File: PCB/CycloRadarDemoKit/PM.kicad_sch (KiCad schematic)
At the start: 47 parts, among them J401 20-16V Supply Voltage, Q401 SI2309CDS, U401 INA3221, U402 RT8259, U403 TPS2121RUXR, U404 AP63205WU, U405 AP63203WU

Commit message: more components fthprnt added
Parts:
- L401: footprint (none) -> Inductor_SMD:L_Changjiang_FNR4018S
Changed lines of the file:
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@@
       (effects (font (size 1.27 1.27)))
     )
-    (property "Footprint" "" (at 125.73 82.55 0)
+    (property "Footprint" "Inductor_SMD:L_Changjiang_FNR4018S" (at 125.73 82.55 0)
       (effects (font (size 1.27 1.27)) hide)
     )

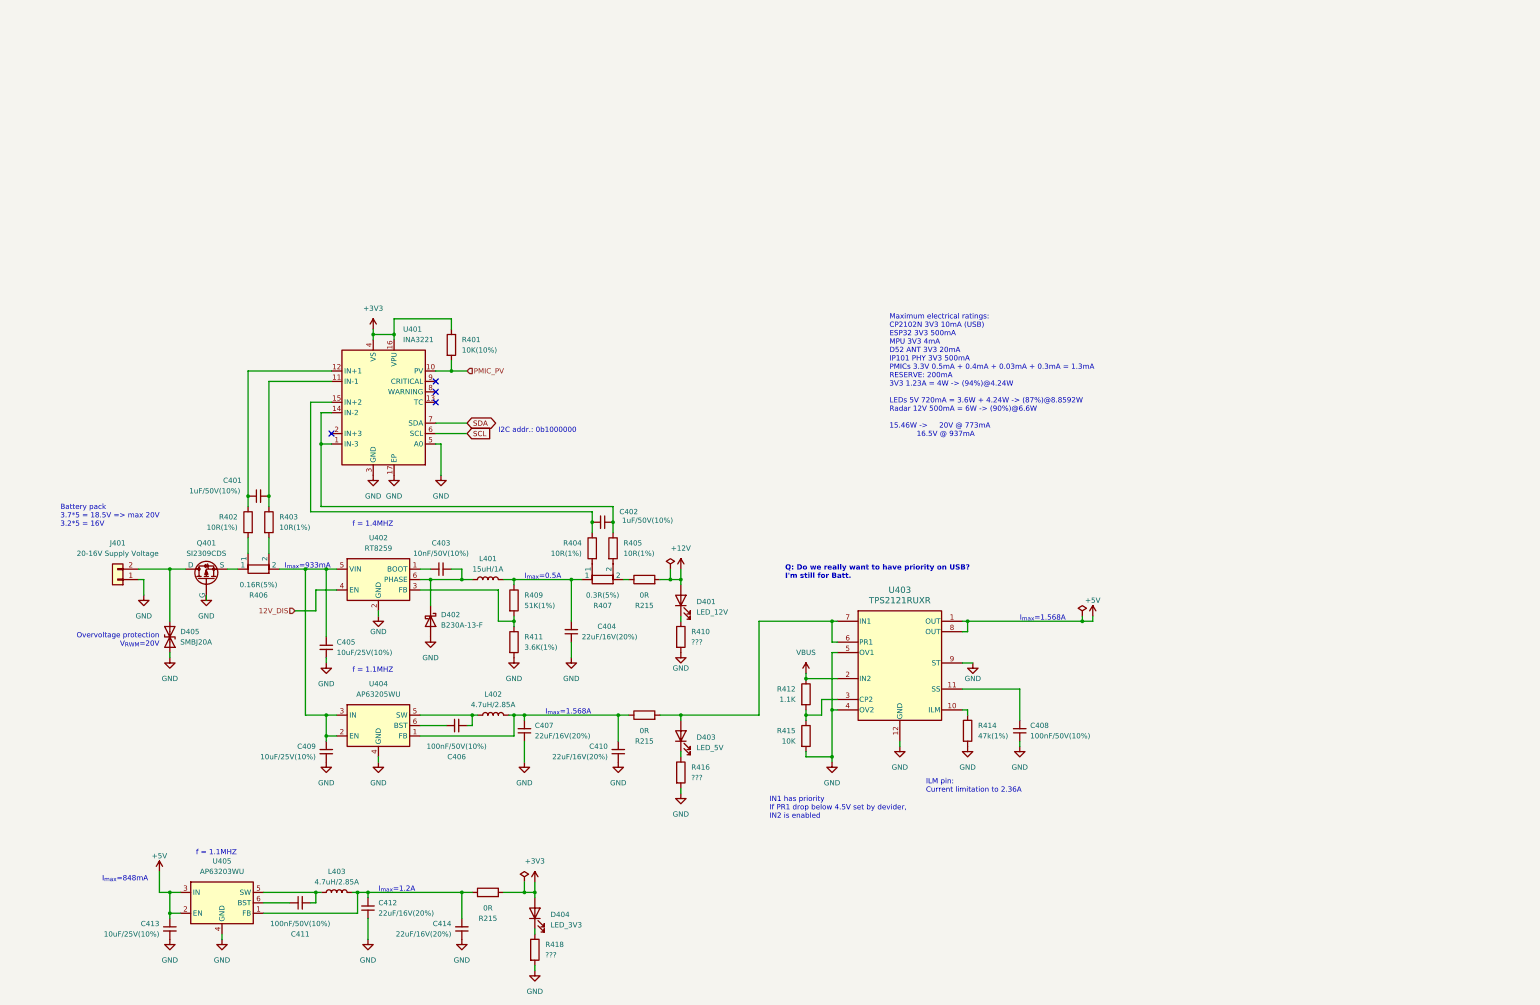
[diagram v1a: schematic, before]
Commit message: added more LCSC parts
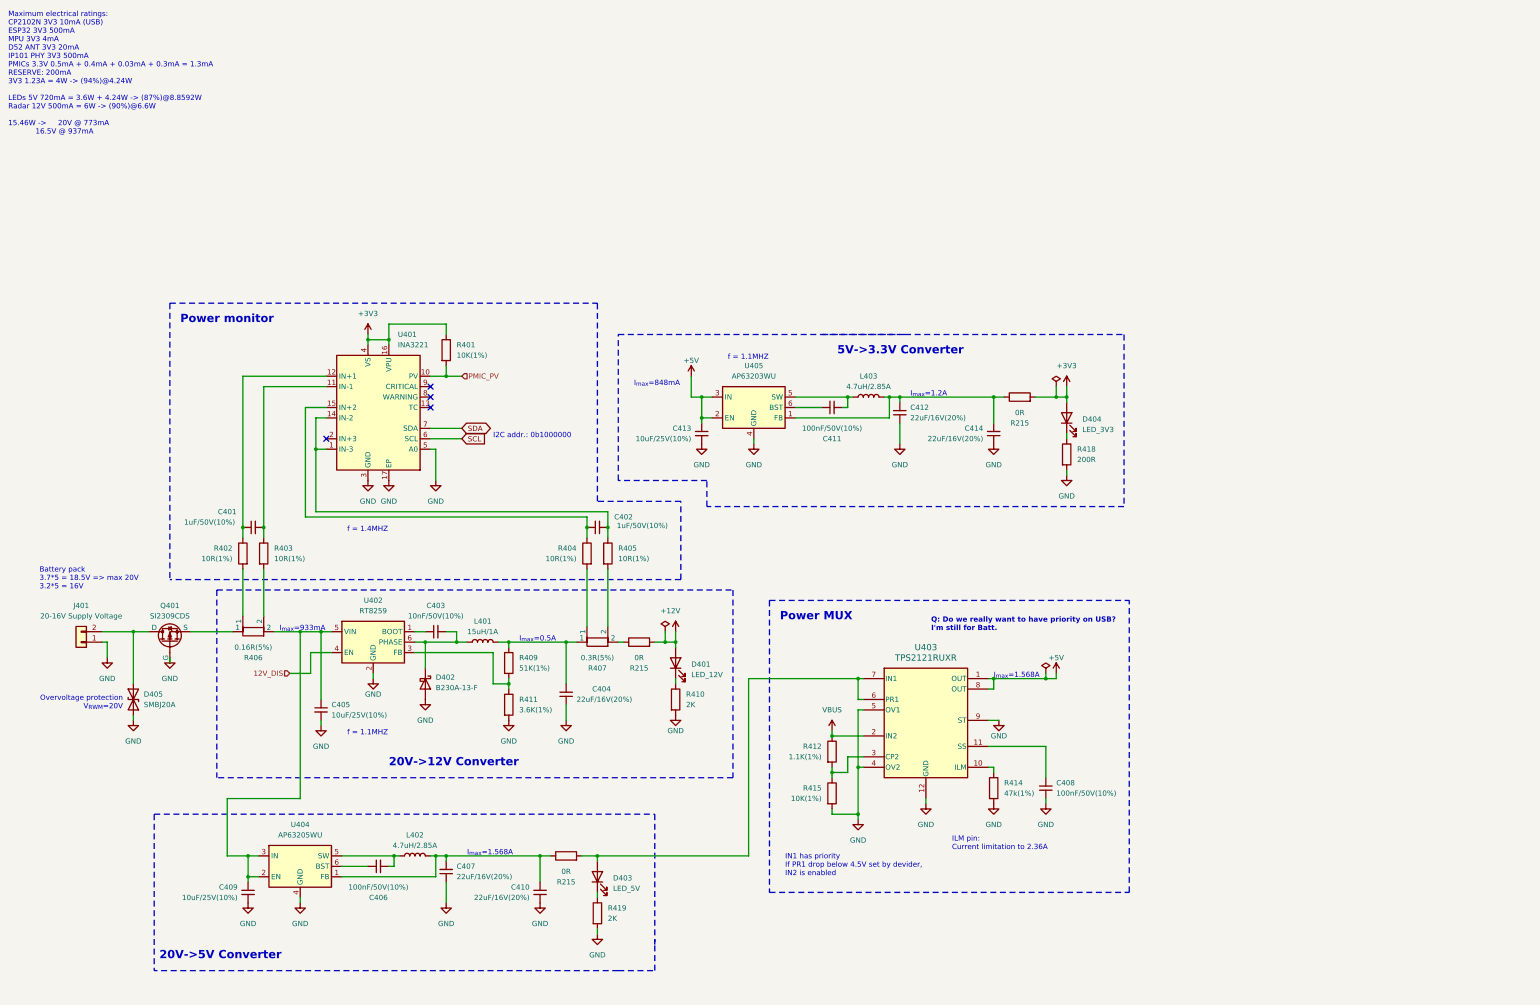
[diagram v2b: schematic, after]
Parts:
- removed R416: ???, symbol Device:R
- added R419: 2K, Resistor_SMD:R_0603_1608Metric, symbol Device:R
- D401: footprint (none) -> LED_SMD:LED_0603_1608Metric; LCSC (none) -> C284922
- D403: footprint (none) -> LED_SMD:LED_0603_1608Metric; LCSC (none) -> C87326
- D404: footprint (none) -> LED_SMD:LED_0603_1608Metric; LCSC (none) -> C497937
- R401: value 10K(10%) -> 10K(1%); footprint (none) -> Resistor_SMD:R_0603_1608Metric; LCSC (none) -> C25804
- R402, R403, R404, R405: footprint (none) -> Capacitor_SMD:C_0603_1608Metric; LCSC (none) -> C22859
- R410: value ??? -> 2K; footprint (none) -> Resistor_SMD:R_0603_1608Metric; LCSC (none) -> C22764
- R412: value 1.1K -> 1.1K(1%); footprint (none) -> Resistor_SMD:R_0603_1608Metric; LCSC (none) -> C22764
- R414: LCSC 0603 -> C25819
- R415: value 10K -> 10K(1%); footprint (none) -> Resistor_SMD:R_0603_1608Metric; LCSC (none) -> C25804
- R418: value ??? -> 200R; footprint (none) -> Resistor_SMD:R_0603_1608Metric; LCSC (none) -> C8218
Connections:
- net GND: now also R419.2
- net at D403.1 (K): now also R419.1
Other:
- note added: "20V->12V Converter"
- note added: "20V->5V Converter"
- note added: "5V->3.3V Converter"
- note added: "Power MUX"
- note added: "Power monitor"
- moved on the sheet: C401, C402, C403, C404, C405, C406, C407, C408, C409, C410, C411, C412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

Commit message: PCB ready for review
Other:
- note added: "Recomended sense filtration"
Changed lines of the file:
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@@
     (effects (font (size 1.27 1.27)) (justify right bottom))
   )
-  (text "f = 1.4MHZ" (at 91.44 71.12 0)
+  (text "f = 1.4MHZ" (at 135.89 129.54 0)
     (effects (font (size 1.27 1.27)) (justify left bottom))
   )
   (text "Maximum electrical ratings:\nCP2102N 3V3 10mA (USB)\nESP32 3V3 500mA\nMPU 3V3 4mA\nD52 ANT 3V3 20mA\nIP101 PHY 3V3 500mA\nPMICs 3.3V 0.5mA + 0.4mA + 0.03mA + 0.3mA = 1.3mA\nRESERVE: 200mA\n3V3 1.23A = 4W -> (94%)@4.24W\n\nLEDs 5V 720mA = 3.6W + 4.24W -> (87%)@8.8592W\nRadar 12V 500mA = 6W -> (90%)@6.6W \n\n15.46W -> 	20V @ 773mA\n			16.5V @ 937mA\n\n\n"
-    (at 8.89 -21.59 0)
+    (at 300.99 58.42 0)
     (effects (font (size 1.27 1.27)) (justify left bottom))
   )
@@
     (effects (font (size 1.27 1.27)) (justify left bottom))
   )
-  (text "f = 1.1MHZ" (at 184.15 29.21 0)
+  (text "f = 1.1MHZ" (at 181.61 63.5 0)
     (effects (font (size 1.27 1.27)) (justify left bottom))
   )
@@
     (effects (font (size 1.27 1.27)) (justify left bottom))
   )
+  (text "f = 1.1MHZ" (at 78.74 176.53 0)
+    (effects (font (size 1.27 1.27)) (justify left bottom))
+  )
   (text "I_{max}=1.2A" (at 228.6 38.1 0)
     (effects (font (size 1.27 1.27)) (justify left bottom))
   )
+  (text "Recomended sense filtration" (at 83.82 76.2 0)
+    (effects (font (size 1.27 1.27)) (justify left bottom))
+  )

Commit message: PCB after review
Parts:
- added R215: NC, Resistor_SMD:R_0805_2012Metric, symbol Device:R
- added R215: 0R, Resistor_SMD:R_0805_2012Metric, symbol Device:R
- C401: renamed from C411; footprint Capacitor_SMD:C_0805_2012Metric -> Capacitor_SMD:C_0603_1608Metric; LCSC C2929181 -> C14663
- C410: renamed from C408; footprint Capacitor_SMD:C_0805_2012Metric -> Capacitor_SMD:C_0603_1608Metric; LCSC C2929181 -> C14663
- C411: renamed from C406; footprint Capacitor_SMD:C_0805_2012Metric -> Capacitor_SMD:C_0603_1608Metric; LCSC C2929181 -> C14663
- renumbered C412 to C402, C413 to C403, C414 to C404, C401 to C405, C402 to C406, C403 to C407, C404 to C408, C405 to C409, C407 to C412, C409 to C413, C410 to C414, D404 to D401, D401 to D402, D402 to D403, D405 to D404, D403 to D405, L403 to L401, L401 to L402, L402 to L403, R418 to R403, R402 to R404, R403 to R405, R404 to R406, R405 to R407, R406 to R408, R407 to R409, R409 to R411, R410 to R412, R411 to R414, R412 to R416, R414 to R417, R415 to R418, R419 to R420, U405 to U401, U401 to U402, U402 to U403, U403 to U404, U404 to U405
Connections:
- net GND: now also R215.1
- net at D405.2 (A), R215.2, U404.7 (IN1): now also R215.2; no longer U404.6 (PR1)
- new net: R215.1, R215.2, U404.6 (PR1)
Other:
- note removed: "Q: Do we really want to have priority on USB? I'm still for Batt."
- company: Alps Electric Czech, s.r.o. -> ALPS Electric Czech, s.r.o.
- title: Development module for Radar Safety Sensor -> Safety Ride Radar Sensor
- moved on the sheet: R416, R418

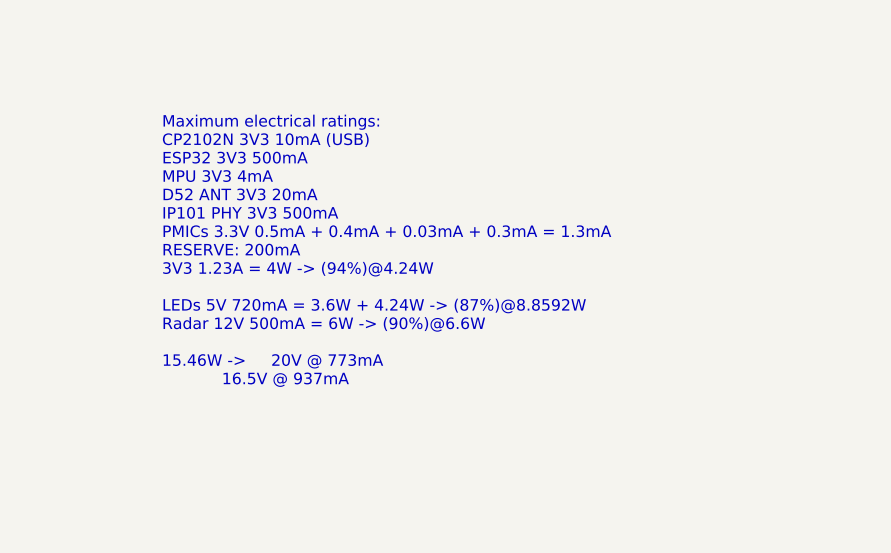
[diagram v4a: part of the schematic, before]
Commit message: schematic cosmetics, power management diagram upgrated
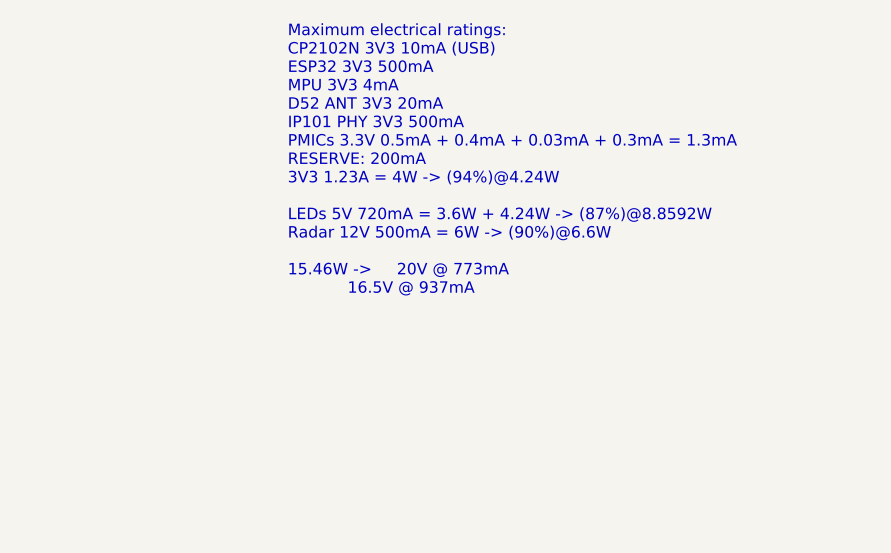
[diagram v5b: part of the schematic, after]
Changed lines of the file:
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@@
   )
   (text "Maximum electrical ratings:\nCP2102N 3V3 10mA (USB)\nESP32 3V3 500mA\nMPU 3V3 4mA\nD52 ANT 3V3 20mA\nIP101 PHY 3V3 500mA\nPMICs 3.3V 0.5mA + 0.4mA + 0.03mA + 0.3mA = 1.3mA\nRESERVE: 200mA\n3V3 1.23A = 4W -> (94%)@4.24W\n\nLEDs 5V 720mA = 3.6W + 4.24W -> (87%)@8.8592W\nRadar 12V 500mA = 6W -> (90%)@6.6W \n\n15.46W -> 	20V @ 773mA\n			16.5V @ 937mA\n\n\n"
-    (at 300.99 58.42 0)
+    (at 314.96 48.26 0)
     (effects (font (size 1.27 1.27)) (justify left bottom))
   )
